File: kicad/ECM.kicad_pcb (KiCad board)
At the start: 2 copper layers, 84.1 x 61.7 mm, 7 parts, among them J1 Bus_PCI_Express_x1, J6 USB_C_Receptacle_USB2.0_16P, U1 MCP25625T-E/ML, U2 RP2040, U4 W25Q128JVP, X1 ABM8-272-T3, Y1 X322516MLB4SI

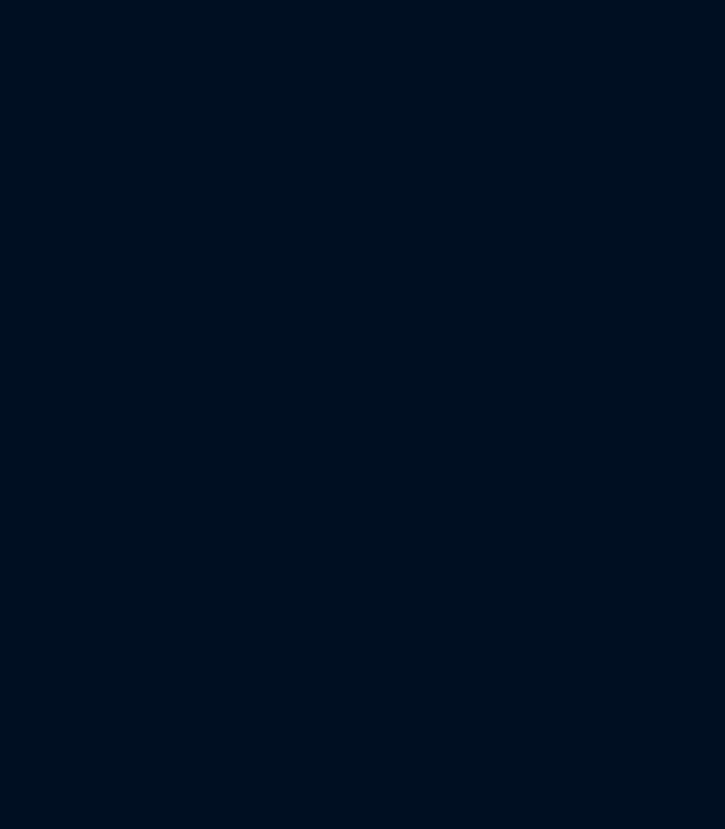
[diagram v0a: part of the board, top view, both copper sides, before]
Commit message: Schematic Capture of RP2040, CAN Network, USB-C, Memory, DAQ, Servo Drivers and PWM Level Shifter.
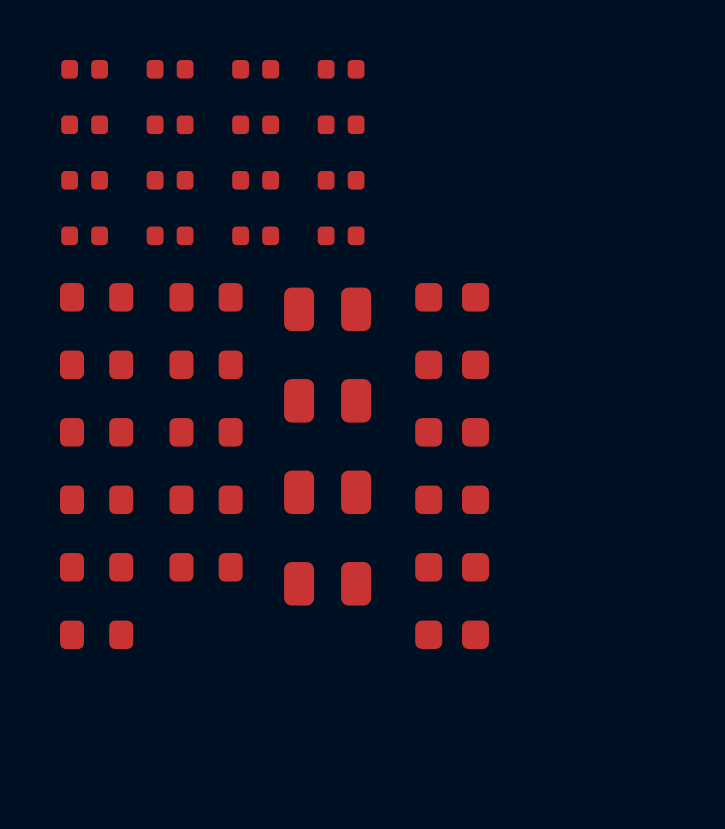
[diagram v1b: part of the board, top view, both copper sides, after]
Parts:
- added C1: 100nF, PCM_JLCPCB:C_0402, F.Cu at (0.93, 0.42)
- added C10: 100nF, PCM_JLCPCB:C_0402, F.Cu at (6.62, 2.27)
- added C11: 1uF, PCM_JLCPCB:C_0402, F.Cu at (6.62, 4.12)
- added C12: 15pF, PCM_JLCPCB:C_0603, F.Cu at (13.2, 8.03)
- added C13: 15pF, PCM_JLCPCB:C_0603, F.Cu at (13.2, 10.3)
- added C14: 100nF, PCM_JLCPCB:C_0402, F.Cu at (6.62, 5.97)
- added C15: 100nF, PCM_JLCPCB:C_0402, F.Cu at (9.47, 0.42)
- added C16: 100nF, PCM_JLCPCB:C_0402, F.Cu at (9.47, 2.27)
- added C17: 100nF, PCM_JLCPCB:C_0402, F.Cu at (9.47, 4.12)
- added C18: 1uF, PCM_JLCPCB:C_0603, F.Cu at (13.2, 12.5)
- added C19: 22pF, PCM_JLCPCB:C_0603, F.Cu at (13.2, 14.8)
- added C2: 100nF, PCM_JLCPCB:C_0402, F.Cu at (0.93, 2.27)
- added C20: 22pF, PCM_JLCPCB:C_0603, F.Cu at (13.2, 17.0)
- added C22: 10uF, PCM_JLCPCB:C_0805, F.Cu at (9.03, 8.43)
- added C23: 1uF, PCM_JLCPCB:C_0402, F.Cu at (9.47, 5.97)
- added C24: 1uF, PCM_JLCPCB:C_0603, F.Cu at (13.2, 19.3)
- added C25: 10uF, PCM_JLCPCB:C_0805, F.Cu at (9.03, 11.5)
- added C26: 10uF, PCM_JLCPCB:C_0805, F.Cu at (9.03, 14.5)
- added C27: 10uF, PCM_JLCPCB:C_0805, F.Cu at (9.03, 17.6)
- added C3: 1uF, PCM_JLCPCB:C_0402, F.Cu at (0.93, 4.12)
- added C4: 100nF, PCM_JLCPCB:C_0402, F.Cu at (0.93, 5.97)
- added C5: 100nF, PCM_JLCPCB:C_0402, F.Cu at (3.77, 0.42)
- added C6: 100nF, PCM_JLCPCB:C_0402, F.Cu at (3.77, 2.27)
- added C7: 100nF, PCM_JLCPCB:C_0402, F.Cu at (3.77, 4.12)
- added C8: 100nF, PCM_JLCPCB:C_0402, F.Cu at (3.77, 5.97)
- added C9: 100nF, PCM_JLCPCB:C_0402, F.Cu at (6.62, 0.42)
- added R1: 1kΩ, PCM_JLCPCB:R_0603, F.Cu at (1.32, 8.03)
- added R10: 5.1kΩ, PCM_JLCPCB:R_0603, F.Cu at (4.97, 14.8)
- added R11: 5.1kΩ, PCM_JLCPCB:R_0603, F.Cu at (4.97, 17.0)
- added R2: 27Ω, PCM_JLCPCB:R_0603, F.Cu at (1.32, 10.3)
- added R3: 27Ω, PCM_JLCPCB:R_0603, F.Cu at (1.32, 12.5)
- added R4: 1kΩ, PCM_JLCPCB:R_0603, F.Cu at (1.32, 14.8)
- added R5: 5.1kΩ, PCM_JLCPCB:R_0603, F.Cu at (1.32, 17.0)
- added R6: 5.1kΩ, PCM_JLCPCB:R_0603, F.Cu at (1.32, 19.3)
- added R7: 5.1kΩ, PCM_JLCPCB:R_0603, F.Cu at (4.97, 8.03)
- added R8: 5.1kΩ, PCM_JLCPCB:R_0603, F.Cu at (4.97, 10.3)
- added R9: 120Ω, PCM_JLCPCB:R_0603, F.Cu at (4.97, 12.5)
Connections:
- net Net-(J6-D+-PadA6) renamed /USB_DP
- net Net-(J6-D--PadA7) renamed /USB_DM
- J6 pad A5: unconnected-(J6-CC1-PadA5) -> Net-(J6-CC1)
- J6 pad B5: unconnected-(J6-CC2-PadB5) -> Net-(J6-CC2)
- U1 pad 1: unconnected-(U1-*CS-Pad1) -> /CS1
- U1 pad 10: unconnected-(U1-RXD-Pad10) -> /RXCAN
- U1 pad 11: unconnected-(U1-VIO-Pad11) -> +3.3V
- U1 pad 12: unconnected-(U1-CANL-Pad12) -> /CANL
- U1 pad 13: unconnected-(U1-CANH-Pad13) -> /CANH
- U1 pad 15: unconnected-(U1-STBY-Pad15) -> /CAN_STBY
- U1 pad 16: unconnected-(U1-TXD-Pad16) -> /TXCAN
- U1 pad 18: unconnected-(U1-VSS-Pad18) -> GND
- U1 pad 19: unconnected-(U1-VDDA-Pad19) -> +5V
- U1 pad 2: unconnected-(U1-*RESET-Pad2) -> Net-(U1-*RESET)
- U1 pad 20: unconnected-(U1-OSC2-Pad20) -> /CAN_OSC2
- U1 pad 21: unconnected-(U1-OSC1-Pad21) -> /CAN_OSC1
- U1 pad 22: unconnected-(U1-GND-Pad22) -> GND
- U1 pad 25: unconnected-(U1-*INT-Pad25) -> /CAN_INT
- U1 pad 26: unconnected-(U1-SCK-Pad26) -> /SCK1
- U1 pad 27: unconnected-(U1-SI-Pad27) -> /SDO1
- U1 pad 28: unconnected-(U1-SO-Pad28) -> /SDI1
- U1 pad 29: unconnected-(U1-EPAD-Pad29) -> GND
- U1 pad 3: unconnected-(U1-VDD-Pad3) -> +3.3V
- U1 pad 4: unconnected-(U1-TXCAN-Pad4) -> /TXCAN
- U1 pad 5: unconnected-(U1-RXCAN-Pad5) -> /RXCAN
- U2 pad 1: Net-(U2-IOVDD-Pad1) -> +3.3V
- U2 pad 10: Net-(U2-IOVDD-Pad1) -> +3.3V
- U2 pad 19: unconnected-(U2-TESTEN-Pad19) -> GND
- U2 pad 20: unconnected-(U2-XIN-Pad20) -> /XIN
- U2 pad 21: unconnected-(U2-XOUT-Pad21) -> /XOUT
- U2 pad 22: Net-(U2-IOVDD-Pad1) -> +3.3V
- U2 pad 23: Net-(U2-DVDD-Pad23) -> +1V1
- U2 pad 24: unconnected-(U2-SWCLK-Pad24) -> /SWCLK
- U2 pad 25: unconnected-(U2-SWD-Pad25) -> /SWD
- U2 pad 26: unconnected-(U2-RUN-Pad26) -> Net-(SW1A-B)
- U2 pad 33: Net-(U2-IOVDD-Pad1) -> +3.3V
- U2 pad 42: Net-(U2-IOVDD-Pad1) -> +3.3V
- U2 pad 43: unconnected-(U2-ADC_AVDD-Pad43) -> +3.3V
- U2 pad 44: unconnected-(U2-VREG_IN-Pad44) -> +3.3V
- U2 pad 45: unconnected-(U2-VREG_VOUT-Pad45) -> +1V1
- U2 pad 46: unconnected-(U2-USB_DM-Pad46) -> Net-(U2-USB_DM)
- U2 pad 47: unconnected-(U2-USB_DP-Pad47) -> Net-(U2-USB_DP)
- U2 pad 48: unconnected-(U2-USB_VDD-Pad48) -> +3.3V
- U2 pad 49: Net-(U2-IOVDD-Pad1) -> +3.3V
- U2 pad 50: Net-(U2-DVDD-Pad23) -> +1V1
- U2 pad 51: unconnected-(U2-QSPI_SD3-Pad51) -> /QSPI_SD3
- U2 pad 52: unconnected-(U2-QSPI_SCLK-Pad52) -> /QSPI_SCLK
- U2 pad 53: unconnected-(U2-QSPI_SD0-Pad53) -> /QSPI_SD0
- U2 pad 54: unconnected-(U2-QSPI_SD2-Pad54) -> /QSPI_SD2
- U2 pad 55: unconnected-(U2-QSPI_SD1-Pad55) -> /QSPI_SD1
- U2 pad 56: unconnected-(U2-QSPI_SS-Pad56) -> /QSPI_SS
- U2 pad 57: unconnected-(U2-GND-Pad57) -> GND
- U4 pad 1: unconnected-(U4-~{CS}-Pad1) -> /QSPI_SS
- U4 pad 2: unconnected-(U4-DO(IO1)-Pad2) -> /QSPI_SD1
- U4 pad 3: unconnected-(U4-IO2-Pad3) -> /QSPI_SD2
- U4 pad 4: unconnected-(U4-GND-Pad4) -> GND
- U4 pad 5: unconnected-(U4-DI(IO0)-Pad5) -> /QSPI_SD0
- U4 pad 6: unconnected-(U4-CLK-Pad6) -> /QSPI_SCLK
- U4 pad 7: unconnected-(U4-IO3-Pad7) -> /QSPI_SD3
- U4 pad 8: unconnected-(U4-VCC-Pad8) -> +3.3V
- X1 pad 1: unconnected-(X1-Pad1) -> /XOUT
- X1 pad 2: unconnected-(X1-Pad2) -> GND
- X1 pad 3: unconnected-(X1-Pad3) -> /XIN
- X1 pad 4: unconnected-(X1-Pad4) -> GND
- Y1 pad 1: unconnected-(Y1-Pad1) -> /CAN_OSC2
- Y1 pad 2: Net-(Y1-Pad2) -> GND
- Y1 pad 3: unconnected-(Y1-Pad3) -> /CAN_OSC1
- Y1 pad 4: Net-(Y1-Pad2) -> GND
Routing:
- added copper zone on F.Cu, net +1V1
- removed copper zone on F.Cu, net unconnected-(U2-VREG_VOUT-Pad45)

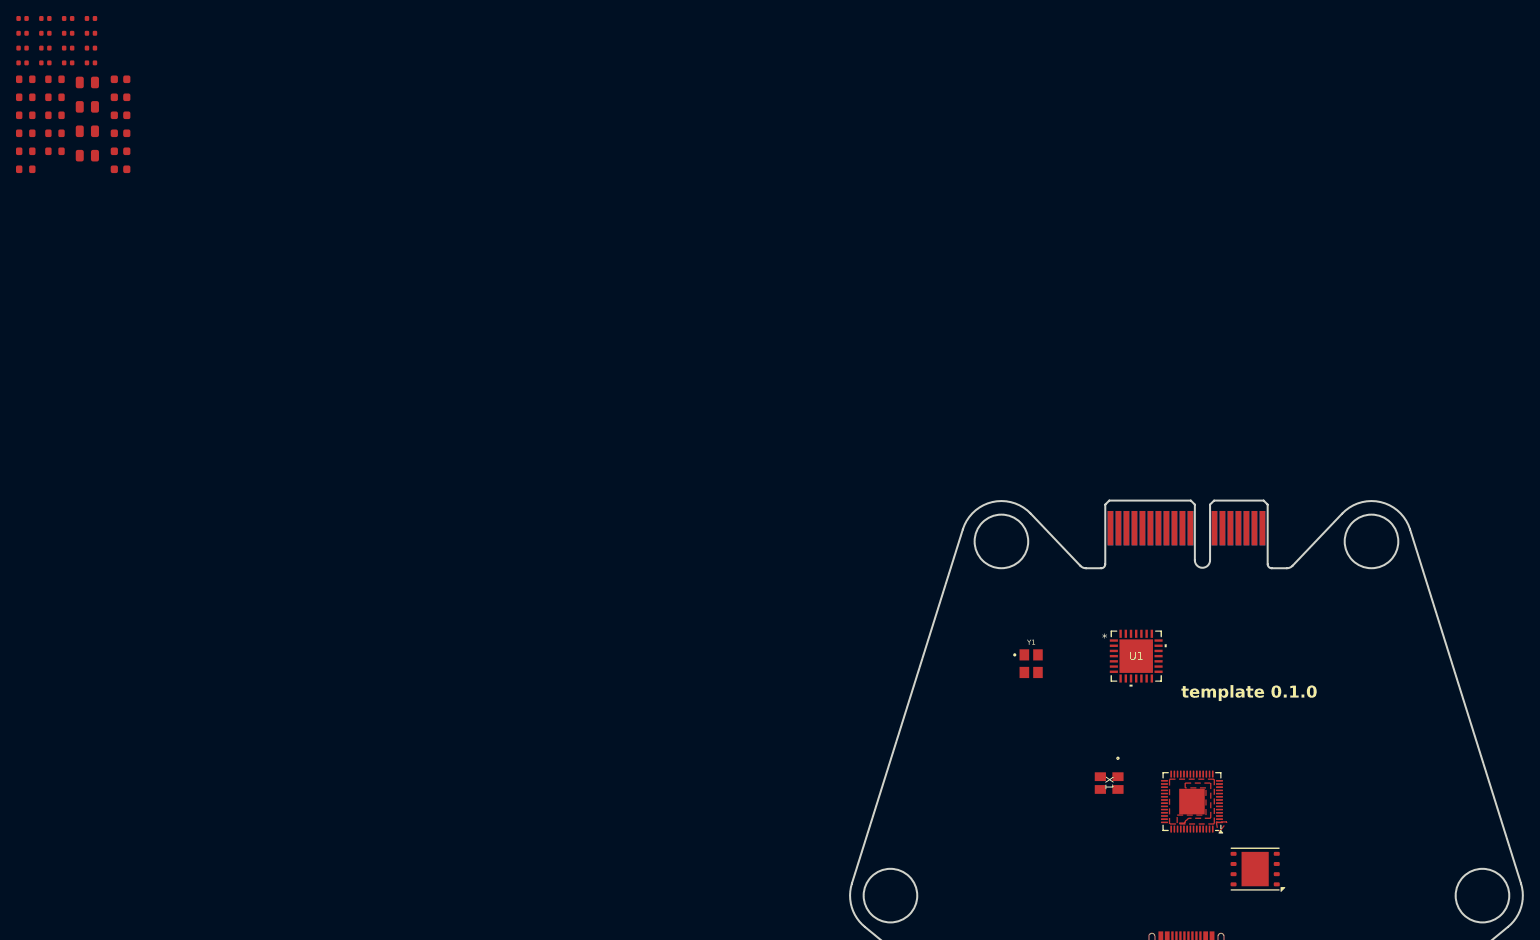
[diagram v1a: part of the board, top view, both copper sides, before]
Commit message: Added thermocouple ICs and dc/dc circuitry for servo power
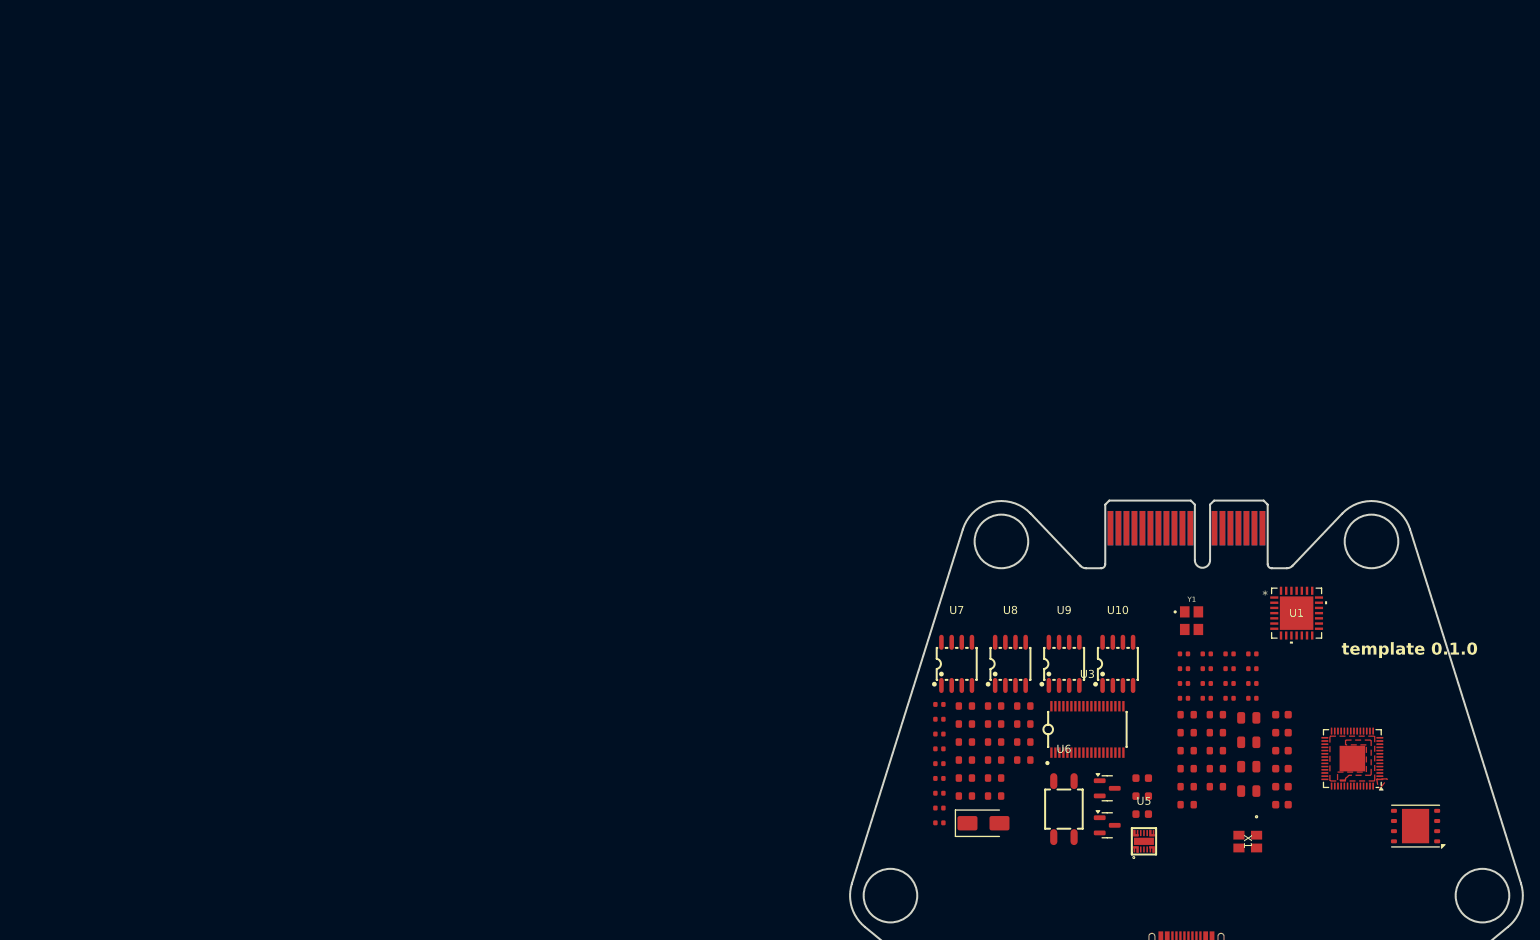
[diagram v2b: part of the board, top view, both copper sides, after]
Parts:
- added C21: 1uF, PCM_JLCPCB:C_0603, F.Cu at (140.9, 95.4)
- added C28: 1uF, PCM_JLCPCB:C_0603, F.Cu at (140.9, 97.6)
- added C29: 100nF, PCM_JLCPCB:C_0402, F.Cu at (115.5, 86.2)
- added C30: 100nF, PCM_JLCPCB:C_0402, F.Cu at (115.5, 88.0)
- added C31: 22nF, PCM_JLCPCB:C_0603, F.Cu at (140.9, 99.9)
- added C32: 100nF, PCM_JLCPCB:C_0402, F.Cu at (115.5, 89.9)
- added C33: 100nF, PCM_JLCPCB:C_0402, F.Cu at (115.5, 91.7)
- added C34: 100nF, PCM_JLCPCB:C_0402, F.Cu at (115.5, 93.6)
- added C35: 100nF, PCM_JLCPCB:C_0402, F.Cu at (115.5, 95.4)
- added D1: SS210, PCM_JLCPCB:D_SMA, F.Cu at (121.0, 101.0)
- added Q1: AO3400A, PCM_JLCPCB:Q_SOT-23, F.Cu at (136.5, 96.7)
- added Q2: AO3400A, PCM_JLCPCB:Q_SOT-23, F.Cu at (136.5, 101.3)
- added R12: 5.1kΩ, PCM_JLCPCB:R_0603, F.Cu at (118.8, 90.9)
- added R13: 5.1kΩ, PCM_JLCPCB:R_0603, F.Cu at (118.8, 93.1)
- added R14: 10Ω, PCM_JLCPCB:R_0603, F.Cu at (118.8, 95.4)
- added R15: 120Ω, PCM_JLCPCB:R_0603, F.Cu at (118.8, 97.6)
- added R16: 5.1kΩ, PCM_JLCPCB:R_0603, F.Cu at (122.4, 86.4)
- added R17: 5.1kΩ, PCM_JLCPCB:R_0603, F.Cu at (122.4, 88.6)
- added R18: 120Ω, PCM_JLCPCB:R_0603, F.Cu at (122.4, 90.9)
- added R19: 5.1kΩ, PCM_JLCPCB:R_0603, F.Cu at (122.4, 93.1)
- added R20: 5.1kΩ, PCM_JLCPCB:R_0603, F.Cu at (122.4, 95.4)
- added R21: 10Ω, PCM_JLCPCB:R_0603, F.Cu at (122.4, 97.6)
- added R22: 10kΩ, PCM_JLCPCB:R_0402, F.Cu at (115.5, 97.3)
- added R23: 10kΩ, PCM_JLCPCB:R_0402, F.Cu at (115.5, 99.1)
- added R24: 10kΩ, PCM_JLCPCB:R_0402, F.Cu at (115.5, 101.0)
- added R25: 5.1kΩ, PCM_JLCPCB:R_0603, F.Cu at (126.1, 86.4)
- added R26: 5.1kΩ, PCM_JLCPCB:R_0603, F.Cu at (126.1, 88.6)
- added R27: 5.1kΩ, PCM_JLCPCB:R_0603, F.Cu at (126.1, 90.9)
- added R28: 5.1kΩ, PCM_JLCPCB:R_0603, F.Cu at (126.1, 93.1)
- added R7: 300Ω, PCM_JLCPCB:R_0603, F.Cu at (118.8, 86.4)
- added R8: 27Ω, PCM_JLCPCB:R_0603, F.Cu at (118.8, 88.6)
- added U10: MAX31855KASA+T, easyeda2kicad:SO-8_L4.9-W3.9-P1.27-LS5.9-BL, F.Cu at (137.8, 81.1)
- added U3: ADS8688IDBTR, easyeda2kicad:TSSOP-38_L9.7-W4.4-P0.50-LS6.4-BL, F.Cu at (134.0, 89.3)
- added U5: TPS22976DPUR, easyeda2kicad:WSON-14_L3.0-W2.0-P0.40-BL-EP-1, F.Cu at (141.1, 103.3)
- added U6: GAQY252G3S, easyeda2kicad:SOP-4_L4.3-W4.4-P2.54-LS7.0-BL, F.Cu at (131.1, 99.3)
- added U7: MAX31855KASA+T, easyeda2kicad:SO-8_L4.9-W3.9-P1.27-LS5.9-BL, F.Cu at (117.7, 81.1)
- added U8: MAX31855KASA+T, easyeda2kicad:SO-8_L4.9-W3.9-P1.27-LS5.9-BL, F.Cu at (124.4, 81.1)
- added U9: MAX31855KASA+T, easyeda2kicad:SO-8_L4.9-W3.9-P1.27-LS5.9-BL, F.Cu at (131.1, 81.1)
- moved C10 165.5 mm to (151.8, 81.7)
- moved C11 165.5 mm to (151.8, 83.5)
- moved C14 165.5 mm to (151.8, 85.4)
- moved C15 165.5 mm to (154.7, 79.8)
- moved C16 165.5 mm to (154.7, 81.7)
- moved C17 165.5 mm to (154.7, 83.5)
- moved C23 165.5 mm to (154.7, 85.4)
- moved C9 165.5 mm to (151.8, 79.8)
- moved R1 165.5 mm to (146.5, 87.5)
- moved R10 165.5 mm to (150.2, 94.2)
- moved R11 165.5 mm to (150.2, 96.5)
- moved R2 165.5 mm to (146.5, 89.7)
- moved R3 165.5 mm to (146.5, 92.0)
- moved R4 165.5 mm to (146.5, 94.2)
- moved R5 165.5 mm to (146.5, 96.5)
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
